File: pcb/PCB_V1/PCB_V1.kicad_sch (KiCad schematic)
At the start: 13 parts, among them U101 TPS54202DDCR

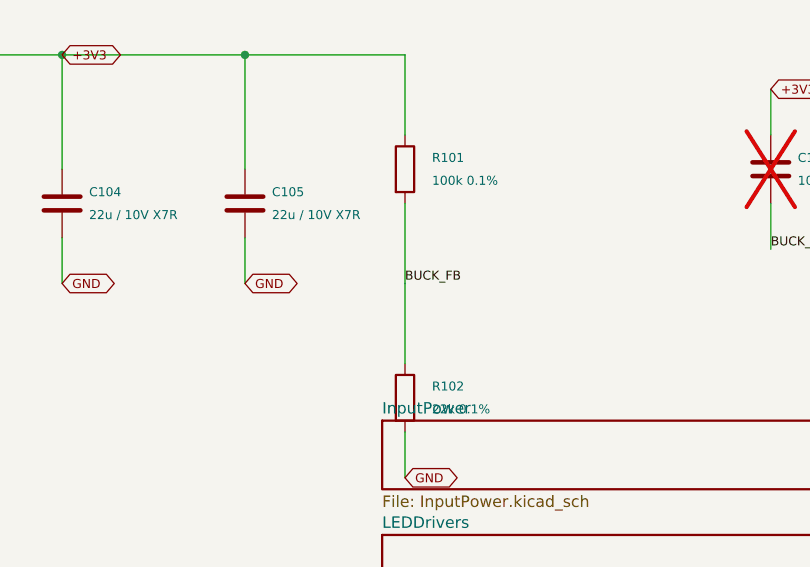
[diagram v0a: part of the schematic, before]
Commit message: pcb: stage four-layer board and enforce unique references
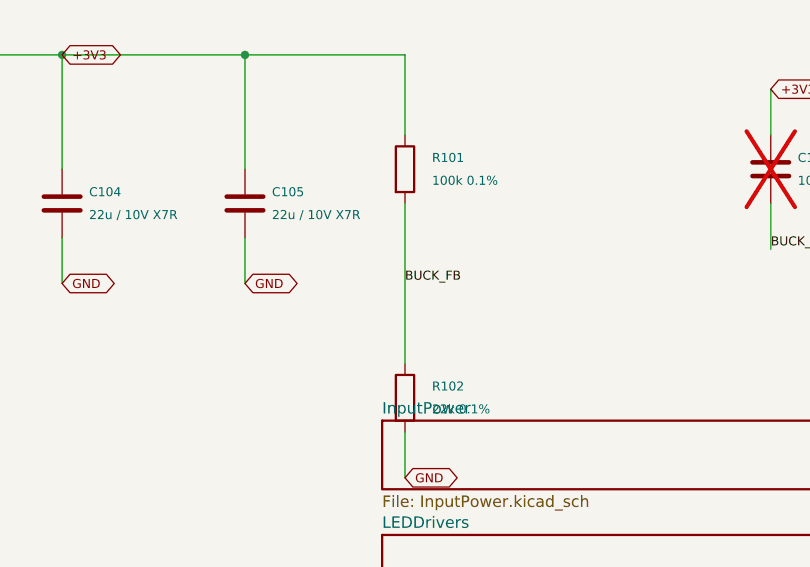
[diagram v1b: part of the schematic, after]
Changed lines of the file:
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@@
-	(wire
-		(pts
-			(xy 203.2 80.01) (xy 203.2 88.9)
-		)
-		(stroke
-			(width 0)
-			(type default)
-		)
-	)
 	(wire
 		(pts
@@
 	(wire
 		(pts
-			(xy 203.2 88.9) (xy 203.2 97.79)
+			(xy 203.2 80.01) (xy 203.2 97.79)
 		)
 		(stroke
@@
 		)
 	)
+	(embedded_fonts no)
 )
